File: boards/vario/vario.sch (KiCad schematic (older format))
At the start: 3 parts

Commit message: PS/2 schematic
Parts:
- gave numbers to parts that had none: 3
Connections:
- net GND: now also J3.3
- net VCC: now also J3.4
- net ps2/ps2_data: now reaches J3.1
- net ps2/ps2_clk: now reaches J3.5
- no-connect marks 7 -> 9
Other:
- moved on the sheet: J3
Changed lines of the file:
@@
 $Descr A2 23386 16535
 encoding utf-8
-Sheet 1 2
+Sheet 1 3
 Title "Various IO module"
 Date "2020-12-23"
@@
 $EndDescr
 $Comp
-L Connector_Generic:Conn_02x20_Odd_Even J?
+L Connector_Generic:Conn_02x20_Odd_Even J1
 U 1 1 5FE386D6
 P 2000 2550
-F 0 "J?" H 2050 3667 50  0000 C CNN
+F 0 "J1" H 2050 3667 50  0000 C CNN
 F 1 "Conn_02x20_Odd_Even" H 2050 3576 50  0000 C CNN
 F 2 "" H 2000 2550 50  0001 C CNN
@@
 $EndComp
 $Comp
-L power:VCC #PWR?
+L power:VCC #PWR01
 U 1 1 5FE3D97F
 P 1800 1650
-F 0 "#PWR?" H 1800 1500 50  0001 C CNN
+F 0 "#PWR01" H 1800 1500 50  0001 C CNN
 F 1 "VCC" V 1815 1777 50  0000 L CNN
 F 2 "" H 1800 1650 50  0001 C CNN
@@
 $EndComp
 $Comp
-L power:GND #PWR?
+L power:GND #PWR03
 U 1 1 5FE3E59A
 P 2300 1650
-F 0 "#PWR?" H 2300 1400 50  0001 C CNN
+F 0 "#PWR03" H 2300 1400 50  0001 C CNN
 F 1 "GND" V 2305 1522 50  0000 R CNN
 F 2 "" H 2300 1650 50  0001 C CNN
@@
 $EndComp
 $Comp
-L power:VCC #PWR?
+L power:VCC #PWR04
 U 1 1 5FE3E980
 P 2300 3550
-F 0 "#PWR?" H 2300 3400 50  0001 C CNN
+F 0 "#PWR04" H 2300 3400 50  0001 C CNN
 F 1 "VCC" V 2315 3678 50  0000 L CNN
 F 2 "" H 2300 3550 50  0001 C CNN
@@
 $EndComp
 $Comp
-L power:GND #PWR?
+L power:GND #PWR02
 U 1 1 5FE3F7E0
 P 1800 3550
-F 0 "#PWR?" H 1800 3300 50  0001 C CNN
+F 0 "#PWR02" H 1800 3300 50  0001 C CNN
 F 1 "GND" V 1805 3422 50  0000 R CNN
 F 2 "" H 1800 3550 50  0001 C CNN
@@
 d7
 $Comp
-L Connector:SD_Card J?
+L Connector:SD_Card J2
 U 1 1 5FE3BA45
 P 17700 6350
-F 0 "J?" H 17700 7015 50  0000 C CNN
+F 0 "J2" H 17700 7015 50  0000 C CNN
 F 1 "SD_Card" H 17700 6924 50  0000 C CNN
 F 2 "" H 17700 6350 50  0001 C CNN
@@
 $EndComp
 $Comp
-L Connector:Mini-DIN-6 J?
+L Connector:Mini-DIN-6 J3
 U 1 1 5FE41893
-P 17700 9650
-F 0 "J?" H 17700 10017 50  0000 C CNN
-F 1 "Mini-DIN-6" H 17700 9926 50  0000 C CNN
-F 2 "" H 17700 9650 50  0001 C CNN
-F 3 "http://service.powerdynamics.com/ec/Catalog17/Section%2011.pdf" H 17700 9650 50  0001 C CNN
-	1    17700 9650
-	1    0    0    -1
+P 7600 2250
+F 0 "J3" H 7600 2617 50  0000 C CNN
+F 1 "Mini-DIN-6" H 7600 2526 50  0000 C CNN
+F 2 "" H 7600 2250 50  0001 C CNN
+F 3 "http://service.powerdynamics.com/ec/Catalog17/Section%2011.pdf" H 7600 2250 50  0001 C CNN
+	1    7600 2250
+	0    1    1    0
 $EndComp
 $Sheet
@@
 F1 "SPI.sch" 50
 $EndSheet
+$Sheet
+S 5600 2000 950  1400
+U 5FE853A4
+F0 "ps2" 50
+F1 "ps2.sch" 50
+F2 "ps2_clk" T R 6550 2850 50
+F3 "ps2_data" T R 6550 2700 50
+F4 "d[0..7]" B L 5600 2150 50
+F5 "~oe" I L 5600 2250 50
+F6 "~we" I L 5600 2350 50
+F7 "~sel" I L 5600 2450 50
+F8 "a" I L 5600 2550 50
+$EndSheet
+Text GLabel 2950 1750 2    50   Input ~ 0
+~rst
+Wire Wire Line
+	2950 1750 2300 1750
+NoConn ~ 7500 1950
+NoConn ~ 7700 1950
+Wire Wire Line
+	6550 2850 7700 2850
+Wire Wire Line
+	7700 2850 7700 2550
+Wire Wire Line
+	6550 2700 7500 2700
+Wire Wire Line
+	7500 2700 7500 2550
+$Comp
+L power:VCC #PWR0101
+U 1 1 6003D229
+P 7600 1950
+F 0 "#PWR0101" H 7600 1800 50  0001 C CNN
+F 1 "VCC" H 7615 2123 50  0000 C CNN
+F 2 "" H 7600 1950 50  0001 C CNN
+F 3 "" H 7600 1950 50  0001 C CNN
+	1    7600 1950
+	1    0    0    -1
+$EndComp
+$Comp
+L power:GND #PWR0102
+U 1 1 6003DAC3
+P 7600 2550
+F 0 "#PWR0102" H 7600 2300 50  0001 C CNN
+F 1 "GND" H 7605 2377 50  0000 C CNN
+F 2 "" H 7600 2550 50  0001 C CNN
+F 3 "" H 7600 2550 50  0001 C CNN
+	1    7600 2550
+	1    0    0    -1
+$EndComp
+Text Label 5600 2150 2    50   ~ 0
+d[0..7]
+Text Label 5600 2250 2    50   ~ 0
+~oe
+Text Label 5600 2350 2    50   ~ 0
+~we
+Text Label 5600 2550 2    50   ~ 0
+a0
+Entry Wire Line
+	4100 2550 4200 2450
+Entry Wire Line
+	4100 2650 4200 2550
+Entry Wire Line
+	4100 2750 4200 2650
+Entry Wire Line
+	4100 2850 4200 2750
+Entry Wire Line
+	4100 2950 4200 2850
+Entry Wire Line
+	4100 3050 4200 2950
+Entry Wire Line
+	4100 3150 4200 3050
+Entry Wire Line
+	4100 3250 4200 3150
+Text Label 3900 3250 2    50   ~ 0
+d7
+Text Label 3900 3150 2    50   ~ 0
+d6
+Text Label 3900 3050 2    50   ~ 0
+d5
+Text Label 3900 2950 2    50   ~ 0
+d4
+Text Label 3900 2850 2    50   ~ 0
+d3
+Text Label 3900 2750 2    50   ~ 0
+d2
+Text Label 3900 2650 2    50   ~ 0
+d1
+Text Label 3900 2550 2    50   ~ 0
+d0
+Wire Wire Line
+	4100 2550 3900 2550
+Wire Wire Line
+	3900 2650 4100 2650
+Wire Wire Line
+	4100 2750 3900 2750
+Wire Wire Line
+	3900 2850 4100 2850
+Wire Wire Line
+	4100 2950 3900 2950
+Wire Wire Line
+	3900 3050 4100 3050
+Wire Wire Line
+	4100 3150 3900 3150
+Wire Wire Line
+	3900 3250 4100 3250
+Wire Bus Line
+	4200 2150 5600 2150
+Wire Bus Line
+	4200 2150 4200 3150
 $EndSCHEMATC

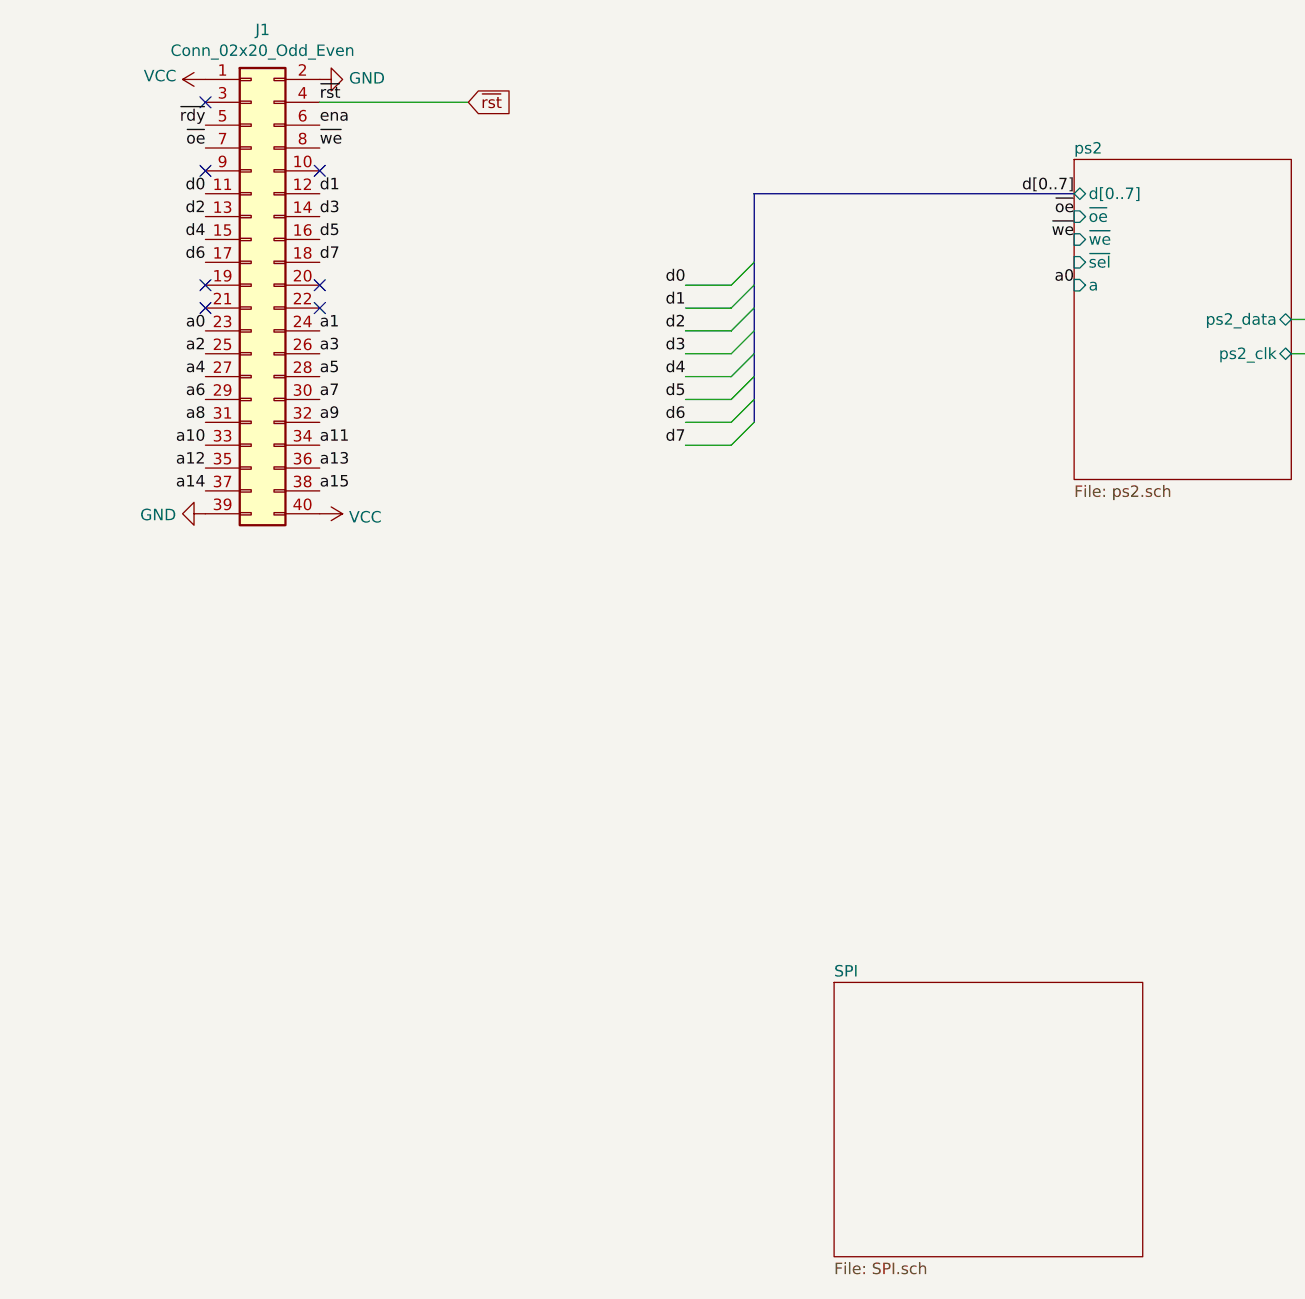
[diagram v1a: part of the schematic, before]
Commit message: SPI: implement missing logic
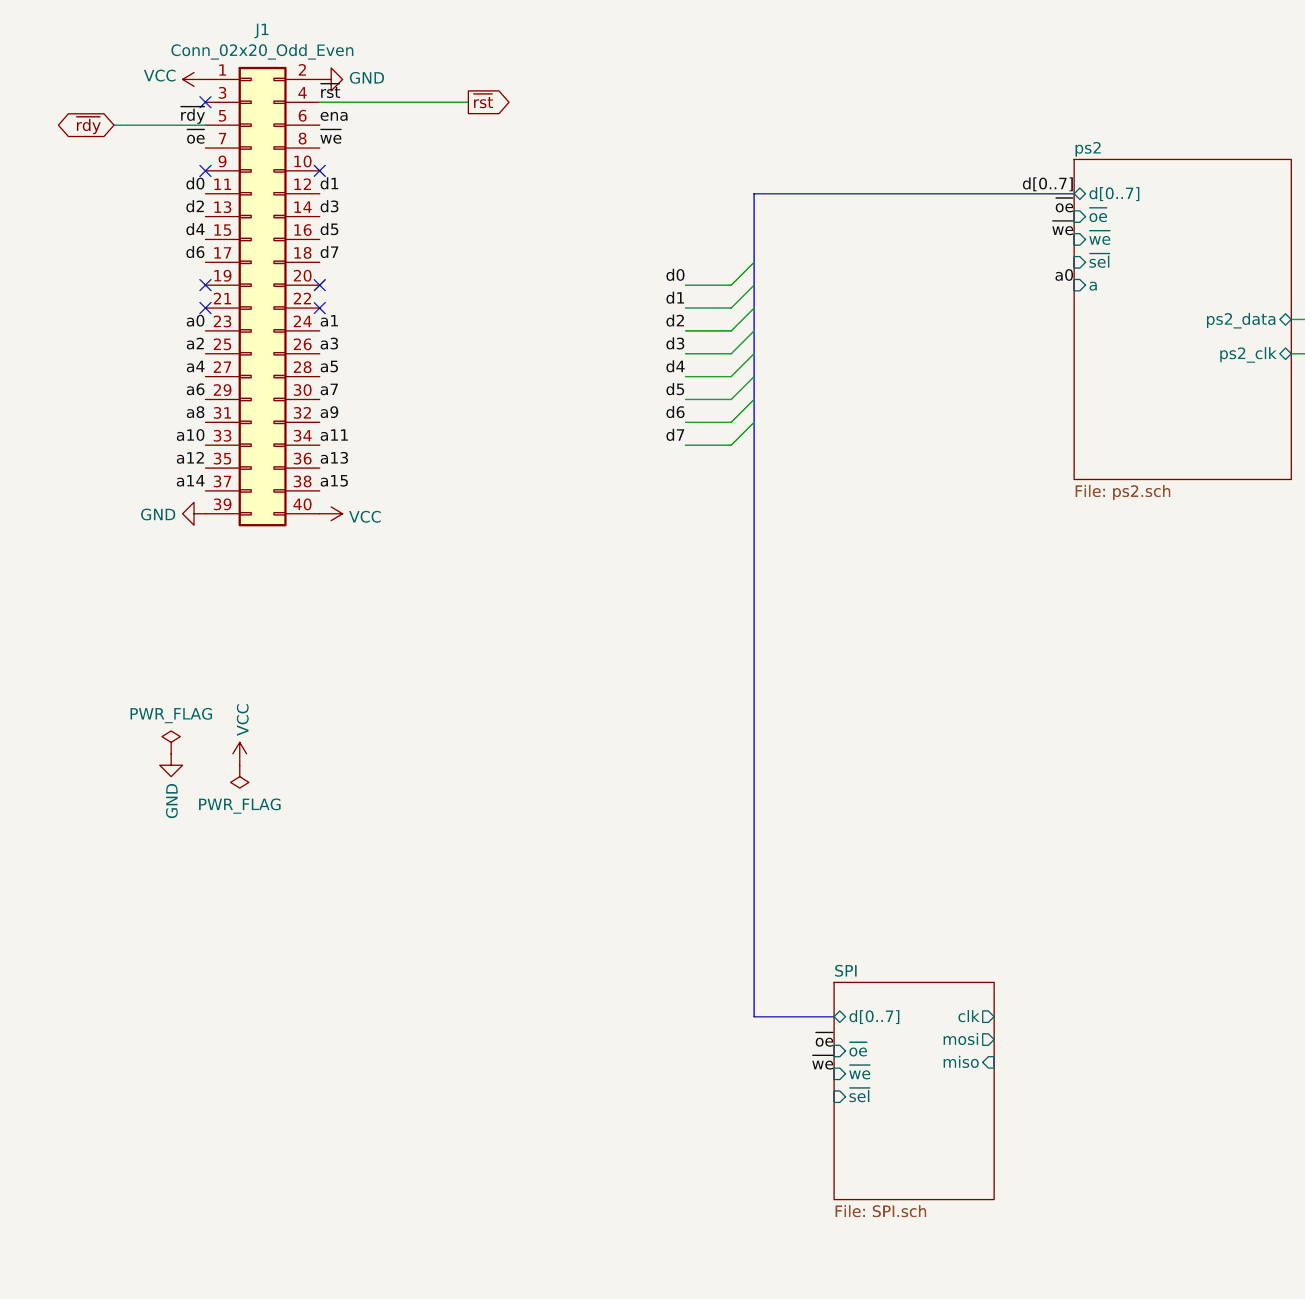
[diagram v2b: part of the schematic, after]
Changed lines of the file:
@@
 $EndComp
 $Sheet
-S 4550 5600 1350 1200
+S 4550 5600 700  950
 U 5FE5ABE2
 F0 "SPI" 50
 F1 "SPI.sch" 50
+F2 "clk" O R 5250 5750 50
+F3 "mosi" O R 5250 5850 50
+F4 "miso" I R 5250 5950 50
+F5 "d[0..7]" B L 4550 5750 50
+F6 "~oe" I L 4550 5900 50
+F7 "~we" I L 4550 6000 50
+F8 "~sel" I L 4550 6100 50
 $EndSheet
 $Sheet
@@
 F8 "a" I L 5600 2550 50
 $EndSheet
-Text GLabel 2950 1750 2    50   Input ~ 0
+Text GLabel 2950 1750 2    50   Output ~ 0
 ~rst
 Wire Wire Line
@@
 Wire Bus Line
 	4200 2150 5600 2150
+Text GLabel 1400 1850 0    50   3State ~ 0
+~rdy
+Wire Wire Line
+	1400 1850 1800 1850
+Text Label 4550 6000 2    50   ~ 0
+~we
+Text Label 4550 5900 2    50   ~ 0
+~oe
 Wire Bus Line
-	4200 2150 4200 3150
+	4550 5750 4200 5750
+Wire Bus Line
+	4200 2150 4200 5750
+$Comp
+L power:PWR_FLAG #FLG0101
+U 1 1 5FF7DC16
+P 1650 4600
+F 0 "#FLG0101" H 1650 4675 50  0001 C CNN
+F 1 "PWR_FLAG" H 1650 4773 50  0000 C CNN
+F 2 "" H 1650 4600 50  0001 C CNN
+F 3 "~" H 1650 4600 50  0001 C CNN
+	1    1650 4600
+	1    0    0    -1
+$EndComp
+$Comp
+L power:GND #PWR0181
+U 1 1 5FF7E163
+P 1650 4600
+F 0 "#PWR0181" H 1650 4350 50  0001 C CNN
+F 1 "GND" V 1655 4472 50  0000 R CNN
+F 2 "" H 1650 4600 50  0001 C CNN
+F 3 "" H 1650 4600 50  0001 C CNN
+	1    1650 4600
+	1    0    0    -1
+$EndComp
+$Comp
+L power:PWR_FLAG #FLG0102
+U 1 1 5FF7E866
+P 1950 4650
+F 0 "#FLG0102" H 1950 4725 50  0001 C CNN
+F 1 "PWR_FLAG" H 1950 4823 50  0000 C CNN
+F 2 "" H 1950 4650 50  0001 C CNN
+F 3 "~" H 1950 4650 50  0001 C CNN
+	1    1950 4650
+	-1   0    0    1
+$EndComp
+$Comp
+L power:VCC #PWR0182
+U 1 1 5FF7EE14
+P 1950 4650
+F 0 "#PWR0182" H 1950 4500 50  0001 C CNN
+F 1 "VCC" V 1965 4778 50  0000 L CNN
+F 2 "" H 1950 4650 50  0001 C CNN
+F 3 "" H 1950 4650 50  0001 C CNN
+	1    1950 4650
+	1    0    0    -1
+$EndComp
 $EndSCHEMATC

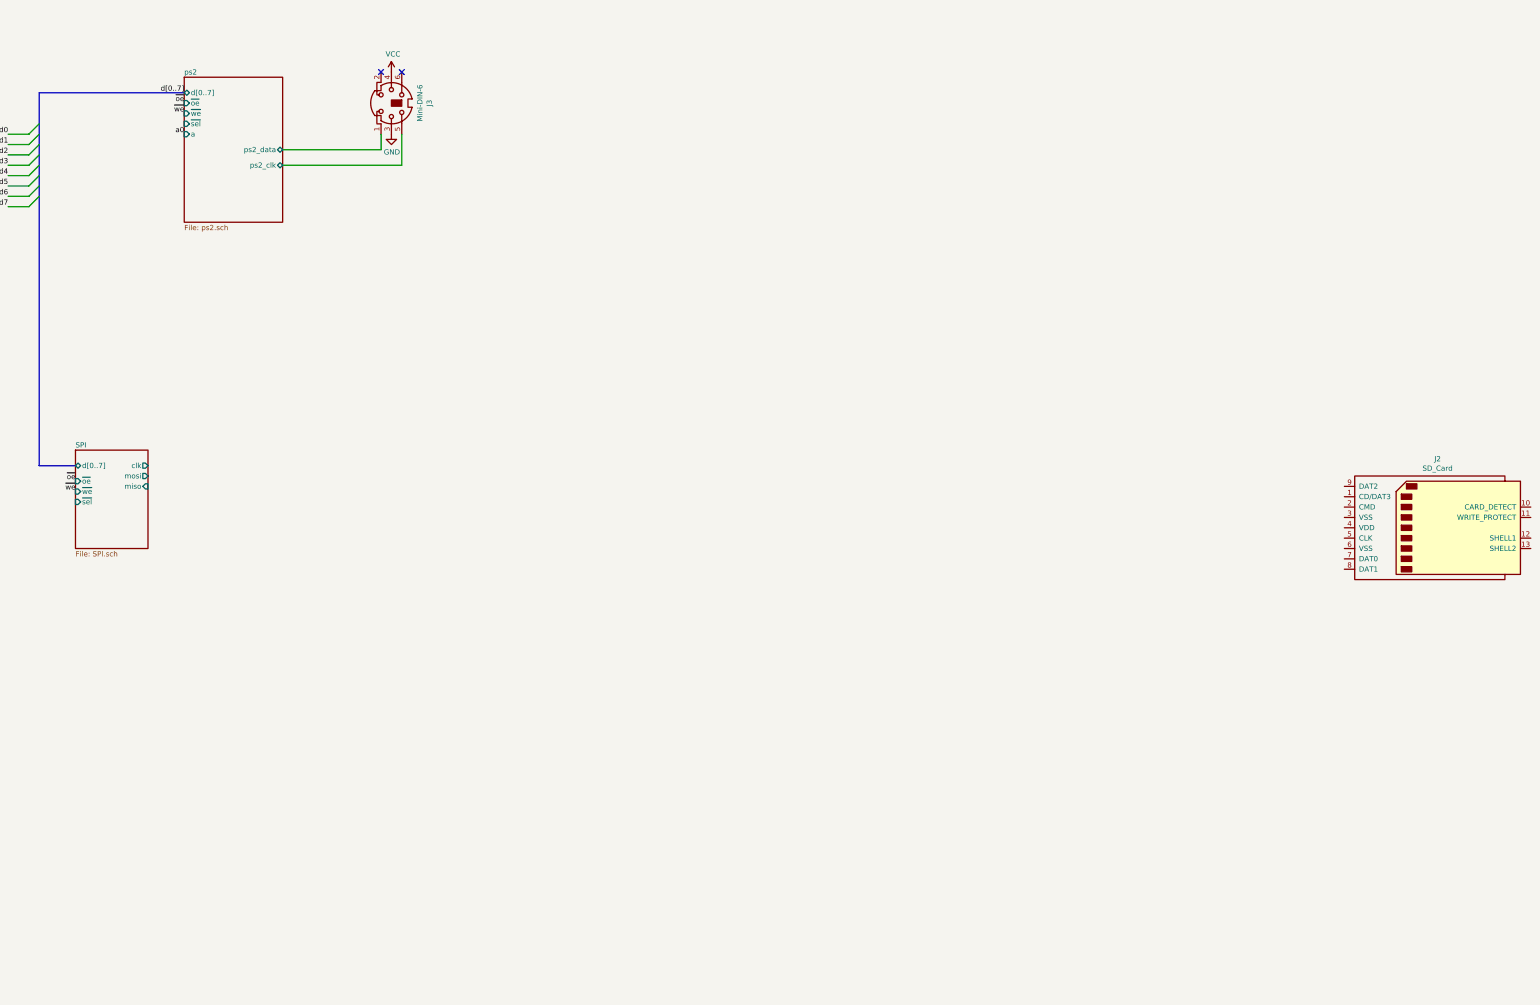
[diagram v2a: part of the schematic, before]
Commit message: Vario: memory card connection and power
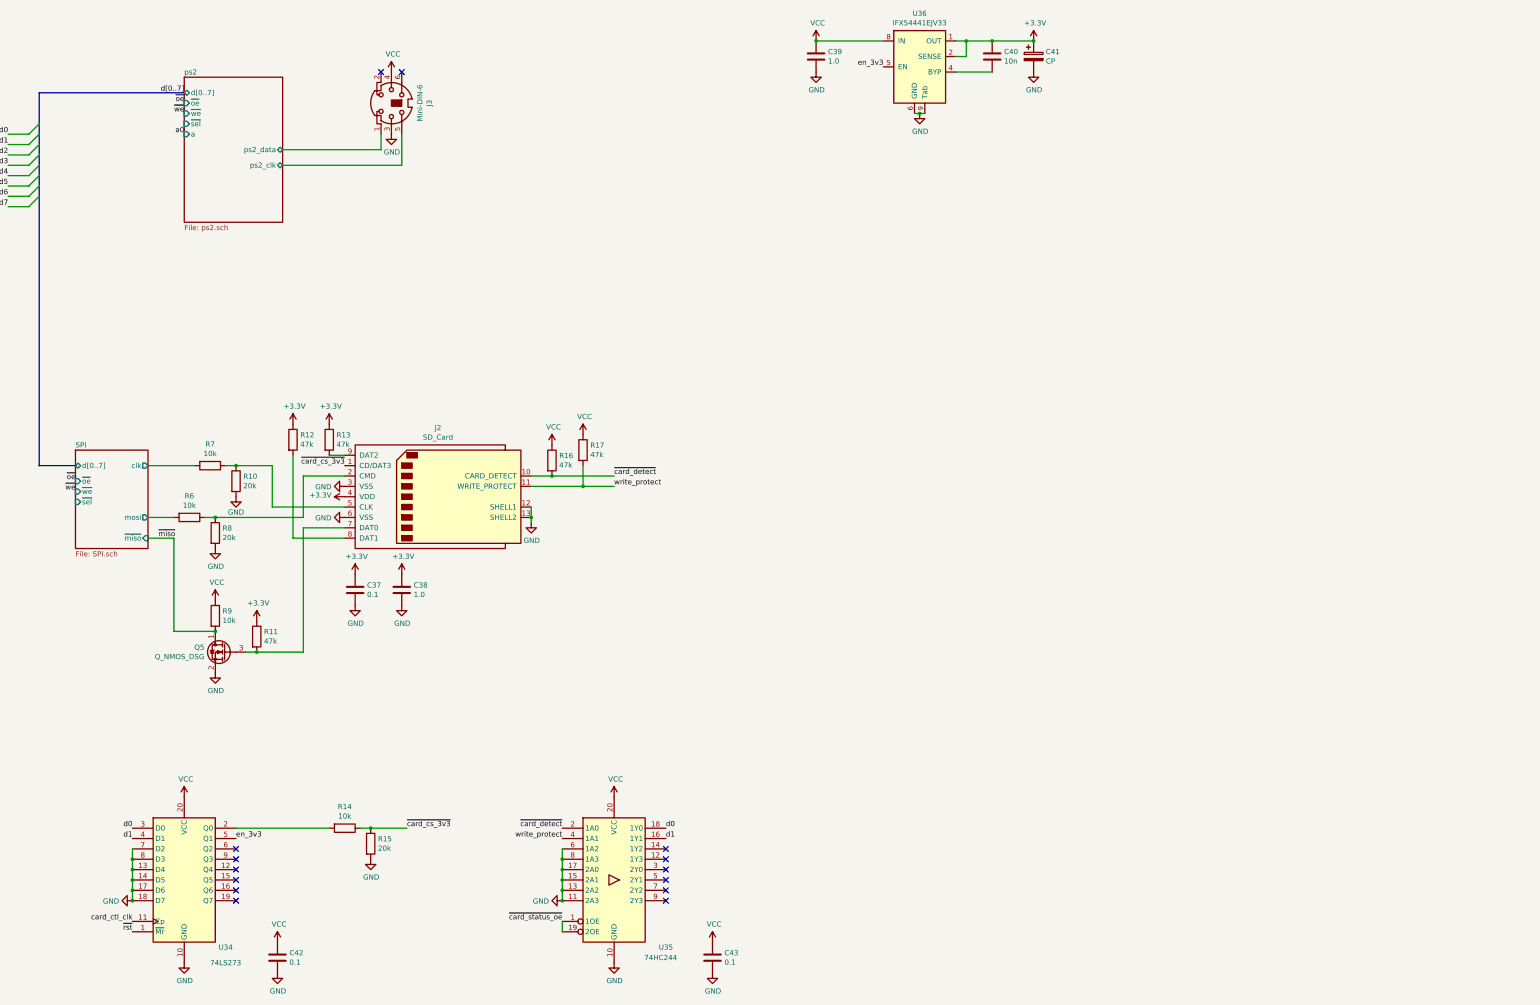
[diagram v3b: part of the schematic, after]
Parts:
- added C37, C42, C43: 0.1, symbol Device:C
- added C38, C39: 1.0, symbol Device:C
- added C40: 10n, symbol Device:C
- added C41: CP, symbol Device:CP
- added Q5: Q_NMOS_DSG, symbol Device:Q_NMOS_DSG
- added R10, R15, R8: 20k, symbol Device:R
- added R11, R12, R13, R16, R17: 47k, symbol Device:R
- added R14, R6, R7, R9: 10k, symbol Device:R
- added U34: 74LS273, symbol 74xx:74LS273
- added U35: 74HC244, symbol 74xx:74HC244
- added U36: IFX54441EJV33, Package_SO:Infineon_PG-DSO-8-27_3.9x4.9mm_EP2.65x3mm, symbol missing:IFX54441EJV33
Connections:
- net GND: now also J2.12 (SHELL1), J2.13 (SHELL2), J2.3 (VSS), J2.6 (VSS), C37.2, C38.2, C39.2, C41.2, C42.2, C43.2, Q5.2 (S), R10.2, R15.2, R8.2, U34.10 (GND), U34.13 (D4), U34.14 (D5), U34.17 (D6), U34.18 (D7), U34.7 (D2), U34.8 (D3), U35.10 (GND), U35.11 (2A3), U35.13 (2A2), U35.15 (2A1), U35.17 (2A0), U35.6 (1A2), U35.8 (1A3), U36.6 (GND), U36.9 (Tab)
- net SPI/clk: now also R7.2
- net SPI/mosi: now also R6.2
- net VCC: now also C39.1, C42.1, C43.1, R16.1, R17.1, R9.1, U34.20 (VCC), U35.20 (VCC), U36.8 (IN)
- net d0: now also U34.3 (D0), U35.18 (1Y0)
- net d1: now also U34.4 (D1), U35.16 (1Y1)
- net ~rst: now also U34.1 (~Mr)
- net ~card_cs_3v3: now reaches J2.1 (CD/DAT3)
- net ~card_cs_3v3: now also R14.1, R15.1
- net ~card_detect: now reaches J2.10 (CARD_DETECT)
- net ~card_detect: now also R16.2, U35.2 (1A0)
- net write_protect: now reaches J2.11 (WRITE_PROTECT)
- net write_protect: now also R17.2, U35.4 (1A1)
- net at J2.2 (CMD): now also R6.1, R8.1
- net +3V3: now reaches J2.4 (VDD)
- net +3V3: now also C37.1, C38.1, C40.1, C41.1, R11.1, R12.1, R13.1, U36.1 (OUT), U36.2 (SENSE)
- net at J2.5 (CLK): now also R10.1, R7.1
- net at J2.7 (DAT0): now also Q5.3 (G), R11.2
- net at J2.8 (DAT1): now also R12.2
- net at J2.9 (DAT2): now also R13.2
- new net: C40.2, U36.4 (BYP)
- new net: R14.2, U34.2 (Q0)
- new net card_ctl_clk: U34.11 (Cp)
- new net en_3v3: U34.5 (Q1), U36.5 (EN)
- new net ~card_status_oe: U35.1 (1OE), U35.19 (2OE)
- new net ~miso: Q5.1 (D), R9.2
- no-connect marks 9 -> 21
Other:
- moved on the sheet: J2
